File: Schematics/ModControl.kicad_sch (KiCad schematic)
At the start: 68 parts, among them J101 Conn_01x04, J102 Conn_01x02, J103 Conn_01x02, J104 Conn_01x02, J105 Conn_01x02, J41 Conn_01x03, J42 Conn_01x03, J89 Conn_01x03, Q12 BSS138, Q13 BSS138, Q16 BSS138, Q17 BSS138, U102 LM78L05, U103 DG212C, U104 AMS1117-3.3, U42 LM324, U51 PCF8575, U52 ADS1115IDGS, U93 DG212C, U94 DG212C, U98 DG212C

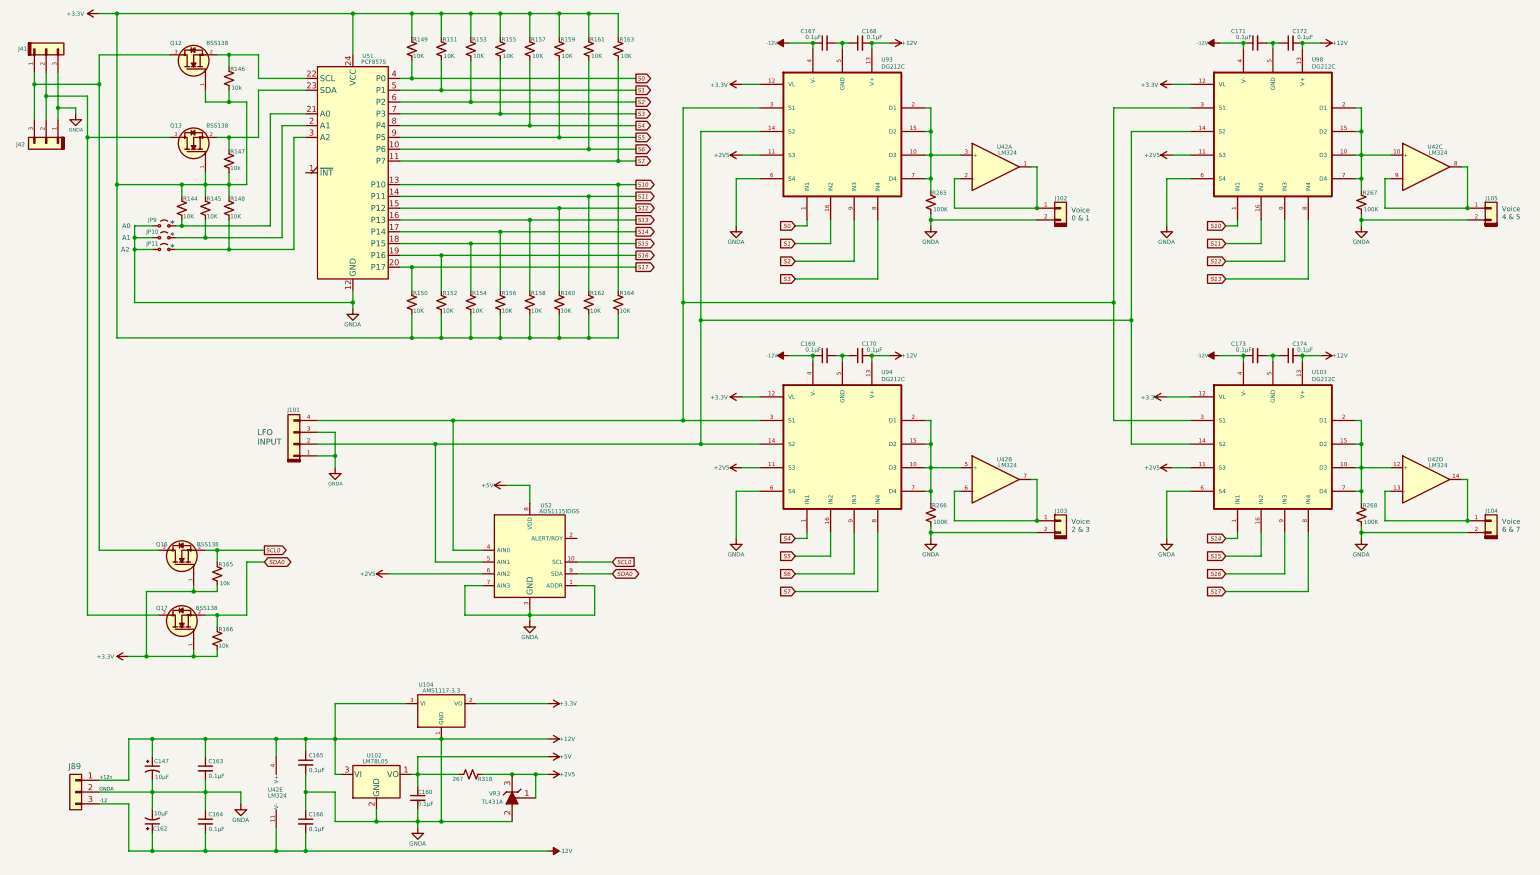
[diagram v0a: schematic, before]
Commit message: minor adjustments for modulation control interface.
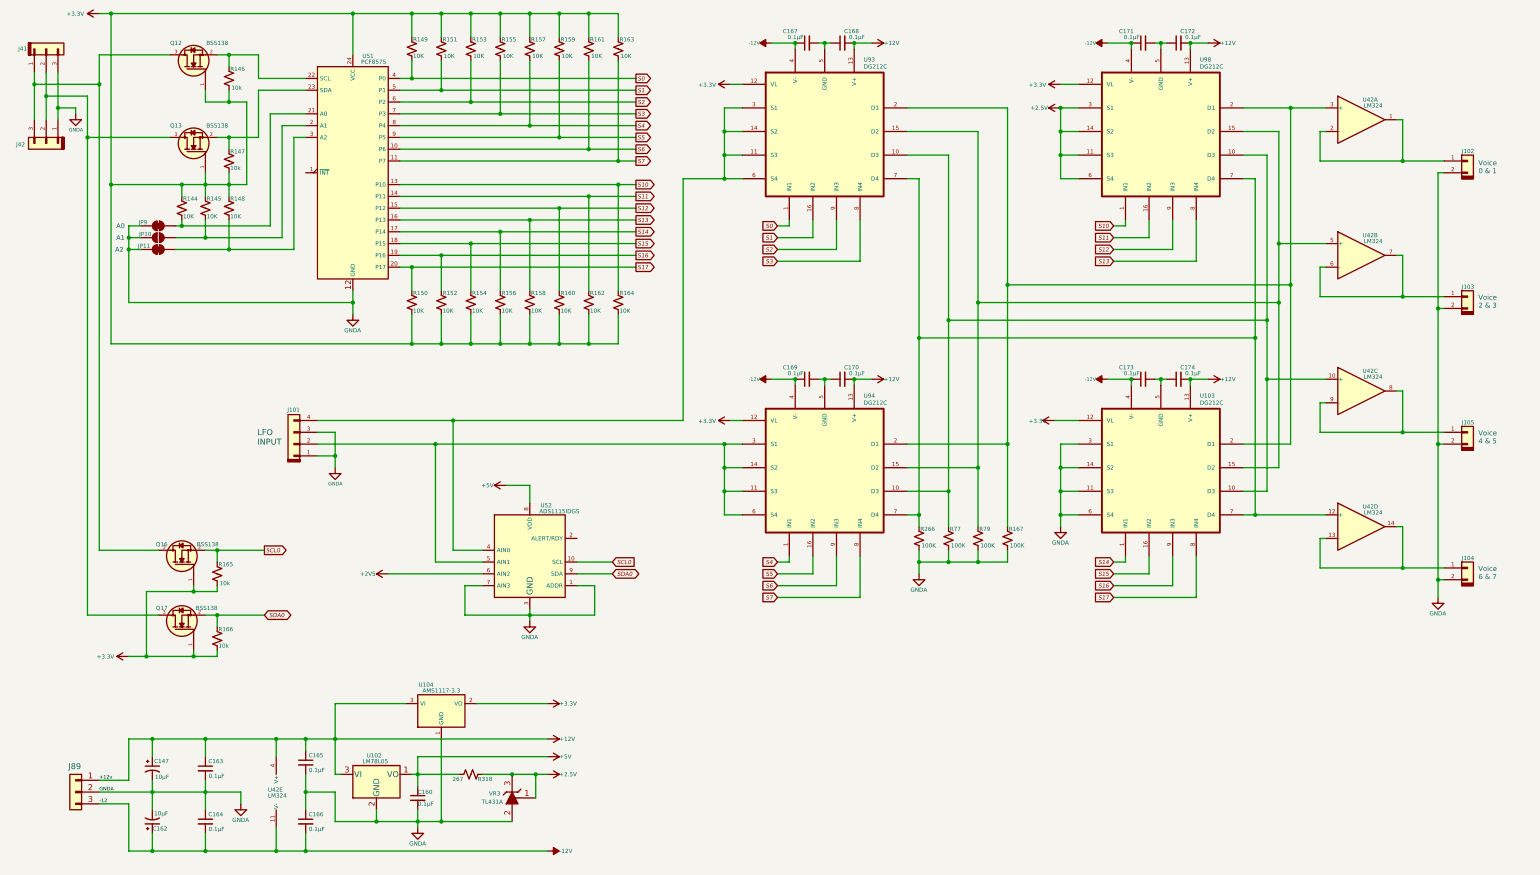
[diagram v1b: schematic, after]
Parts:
- removed JP10, JP11, JP9: Jumper_2_Small_Open, symbol Jumper:Jumper_2_Small_Open
- removed R265, R267, R268: 100K, symbol Device:R_Small_US
- added JP10: SolderJumper_2_Open, symbol Jumper:SolderJumper_2_Open
- added JP11, JP9: ~, symbol Jumper:SolderJumper_2_Bridged
- added R167, R266, R77: 100K, symbol Device:R_Small_US
- renumbered R266 to R79
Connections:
- net +12V: no longer C147.2, C160.2, C162.2, C163.2, C164.1, C165.2, C166.1, J101.1 (Pin_1), J101.3 (Pin_3), J102.2 (Pin_2), J103.2 (Pin_2), J104.2 (Pin_2), J105.2 (Pin_2), J41.3 (Pin_3), J42.1 (Pin_1), J89.2 (Pin_2), R79.2, U102.2 (GND), U103.6 (S4), U104.1 (GND), U51.12 (GND), U52.1 (ADDR), U52.3 (GND), U52.7 (AIN3), U93.6 (S4), U94.6 (S4), U98.6 (S4), VR3.2 (A)
- net +2V5: no longer R318.2, U103.11 (S3), U93.11 (S3), U94.11 (S3), U98.11 (S3), VR3.1 (REF), VR3.3 (K)
- net at R144.2, U51.21 (A0): now also JP9.2 (B)
- net at J101.2 (Pin_2), U52.5 (AIN1), U94.14 (S2): now also U94.11 (S3), U94.3 (S1), U94.6 (S4); no longer U103.14 (S2), U93.14 (S2), U98.14 (S2)
- net at J101.4 (Pin_4), U52.4 (AIN0), U93.3 (S1): now also U93.11 (S3), U93.14 (S2), U93.6 (S4); no longer U103.3 (S1), U94.3 (S1), U98.3 (S1)
- net at R79.1, U42.5 (+), U94.15 (D2): now also U103.15 (D2), U93.15 (D2), U98.15 (D2); no longer U94.10 (D3), U94.2 (D1), U94.7 (D4)
- net at R148.2, U51.3 (A2): now also JP11.2 (B)
- net at R145.2, U51.2 (A1): now also JP10.2 (B)
- new net: R167.1, U103.2 (D1), U42.3 (+), U93.2 (D1), U94.2 (D1), U98.2 (D1)
- new net: R77.1, U103.10 (D3), U42.10 (+), U93.10 (D3), U94.10 (D3), U98.10 (D3)
- new net: R266.1, U103.7 (D4), U42.12 (+), U93.7 (D4), U94.7 (D4), U98.7 (D4)
- new net +2.5V: R318.2, U98.11 (S3), U98.14 (S2), U98.3 (S1), U98.6 (S4), VR3.1 (REF), VR3.3 (K)
- new net GNDA: C147.2, C160.2, C162.2, C163.2, C164.1, C165.2, C166.1, J101.1 (Pin_1), J101.3 (Pin_3), J102.2 (Pin_2), J103.2 (Pin_2), J104.2 (Pin_2), J105.2 (Pin_2), J41.3 (Pin_3), J42.1 (Pin_1), J89.2 (Pin_2), JP10.1 (A), JP11.1 (A), JP9.1 (A), R167.2, R266.2, R77.2, R79.2, U102.2 (GND), U103.11 (S3), U103.14 (S2), U103.3 (S1), U103.6 (S4), U104.1 (GND), U51.12 (GND), U52.1 (ADDR), U52.3 (GND), U52.7 (AIN3), VR3.2 (A)
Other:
- note removed: "*"
- moved on the sheet: C167, C168, C169, C170, C171, C172, C173, C174, J102, J103, J104, J105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

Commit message: Added support hardware for LFO output matrix and calibration analog to digital converter.
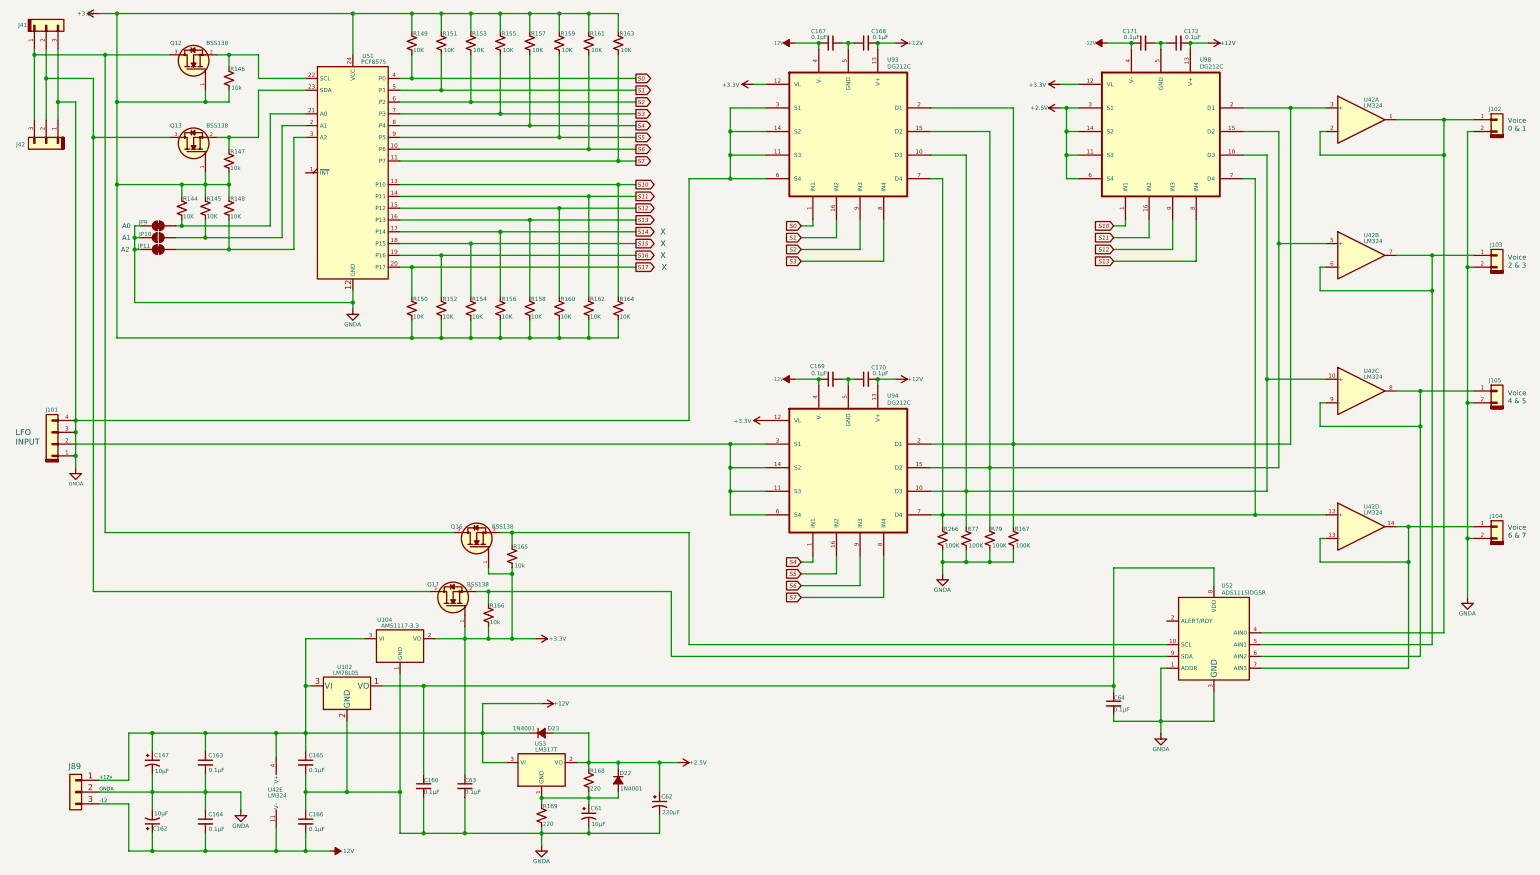
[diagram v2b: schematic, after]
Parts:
- removed C173, C174: 0.1µF, symbol Device:C_Small
- removed R318: 267, symbol Device:R_Small_US
- removed U103: DG212C, symbol My Chips:DG212C
- removed VR3: TL431A, digikey-footprints:TO-92-3_Formed_Leads, symbol dk_PMIC-Voltage-Reference:TL431CLPM
- added C61: 10µF, symbol Device:C_Polarized_Small_US
- added C62: 220µF, symbol Device:C_Polarized_Small_US
- added C63, C64: 0.1µF, symbol Device:C_Small
- added D22, D23: 1N4001, symbol Device:D_Small_Filled
- added R168, R169: 220, symbol Device:R_Small_US
- added U53: LM317T, Package_TO_SOT_SMD:SOT-223-3_TabPin2, symbol Regulator_Linear:AMS1117-3.3
- U52: value ADS1115IDGS -> ADS1115IDGSR
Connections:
- net +2V5 is gone; now on an unnamed net: U52.6 (AIN2)
- net +12V: now also D23.1 (K), U53.3 (VI)
- net +2.5V: now also C62.1, D22.1 (K), D23.2 (A), R168.1, U53.2 (VO)
- net +3.3V: now also C63.1
- net GNDA: now also J101.4 (Pin_4), U93.11 (S3), U93.14 (S2), U93.3 (S1), U93.6 (S4), C61.2, C62.2, C63.2, C64.2, R169.2; no longer U52.7 (AIN3)
- net at J102.1 (Pin_1), U42.1, U42.2 (-): now also U52.4 (AIN0)
- net at J104.1 (Pin_1), U42.13 (-), U42.14: now also U52.7 (AIN3)
- net at J101.2 (Pin_2), U94.11 (S3), U94.14 (S2)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: no longer U52.5 (AIN1)
- net at J103.1 (Pin_1), U42.6 (-), U42.7: now also U52.5 (AIN1)
- net +5V: no longer names the net of C160.1, U102.1 (VO), U52.8 (VDD)
- net +5V: now also C64.1
- net SCL0: no longer names the net of Q16.2, R165.1, U52.10 (SCL)
- net SDA0: no longer names the net of Q17.2, R166.1, U52.9 (SDA)
- new net: C61.1, D22.2 (A), R168.2, R169.1, U53.1 (GND)
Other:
- note added: "X"
- moved on the sheet: C147, C160, C163, C167, C168, C169, C170, J101, J102, J103, J104, J105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

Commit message: Fixed bugs in voice selection on configuration.  Reorganized schematics to have different master drawings for power and audio paths.  Started work on dual 3-pole state variable filter with resonance.
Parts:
- renumbered C147 to C331, C162 to C332, C163 to C344, C164 to C345, C165 to C359, C166 to C360, C160 to C378, C63 to C384, C61 to C393, C62 to C404, C167 to C419, C169 to C420, C168 to C424, C170 to C425, C64 to C447, C171 to C448, C172 to C451, D23 to D60, D22 to D61, J41 to J211, J42 to J212, J101 to J215, J89 to J227, J102 to J292, J103 to J293, J105 to J294, J104 to J295, JP9 to JP28, JP10 to JP29, JP11 to JP30, Q12 to Q32, Q13 to Q33, Q17 to Q38, Q16 to Q39, R144 to R571, R145 to R578, R146 to R584, R147 to R585, R148 to R586, R149 to R622, R150 to R623, R151 to R631, R152 to R632, R153 to R637, R154 to R638, R166 to R641, R155 to R645, R156 to R646, R165 to R649, R157 to R658, R158 to R659, R169 to R667, R159 to R671, R160 to R672, R161 to R682, R162 to R683, R168 to R684, R163 to R690, R164 to R691, R266 to R734, R77 to R738, R79 to R747, R167 to R749, U42 to U214, U102 to U224, U51 to U225, U104 to U228, U53 to U244, U93 to U265, U94 to U266, U98 to U288, U52 to U295
